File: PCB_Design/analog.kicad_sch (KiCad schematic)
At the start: 27 parts, among them U18 AD7680ARJZ-REEL7, U19 TL071, U20 TL071, U21 INA849DR, U22 AD630ARZ, U23 TL071

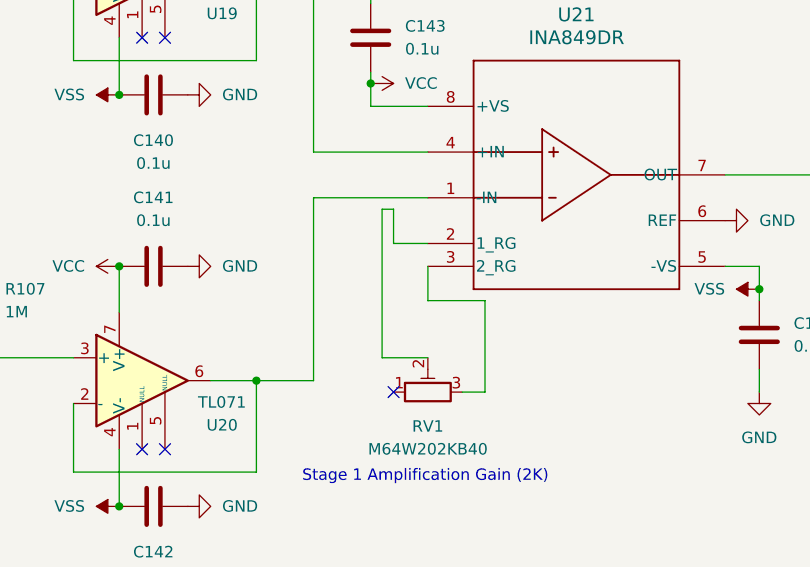
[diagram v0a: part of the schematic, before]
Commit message: KiCAD file update, completed PCB
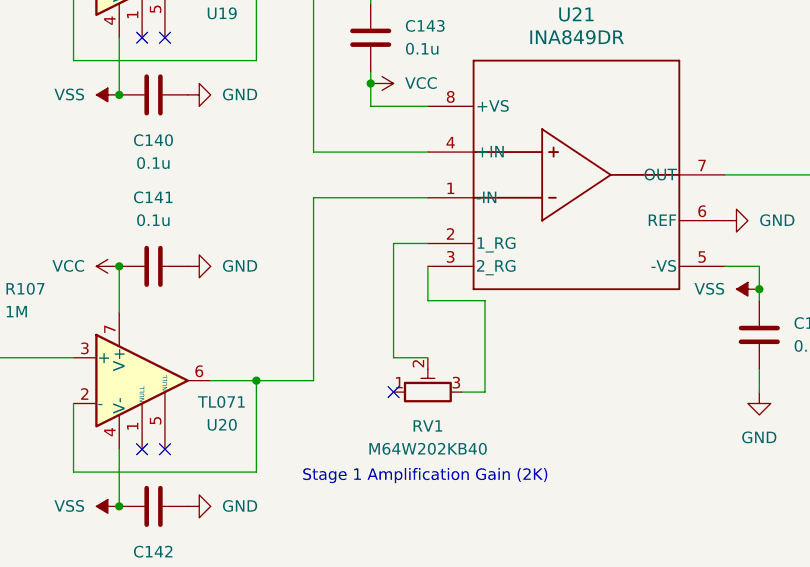
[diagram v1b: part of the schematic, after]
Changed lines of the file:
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@@
-    (stroke (width 0) (type default))
-  )
-  (wire (pts (xy 97.79 78.74) (xy 97.79 82.55))
     (stroke (width 0) (type default))
   )
@@
     (stroke (width 0) (type default))
   )
-  (wire (pts (xy 96.52 78.74) (xy 97.79 78.74))
-    (stroke (width 0) (type default))
-  )
   (wire (pts (xy 274.32 73.66) (xy 267.97 73.66))
     (stroke (width 0) (type default))
@@
     (stroke (width 0) (type default))
   )
-  (wire (pts (xy 96.52 95.25) (xy 101.6 95.25))
+  (wire (pts (xy 97.79 95.25) (xy 101.6 95.25))
     (stroke (width 0) (type default))
   )
@@
     (stroke (width 0) (type default))
   )
-  (wire (pts (xy 96.52 78.74) (xy 96.52 95.25))
+  (wire (pts (xy 97.79 82.55) (xy 97.79 95.25))
     (stroke (width 0) (type default))
   )
